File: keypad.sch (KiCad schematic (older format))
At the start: 19 parts, among them J1 Conn_01x04_Female, J3 B3FS-1002P, J4 USB_C_Receptacle_USB2.0, U1 ATMEGA32U4, Y1 Crystal_GND24

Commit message: first manufactured version, testing needed
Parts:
- J4: footprint Connector_USB:USB_C_Receptacle_Amphenol_12401548E4-2A_CircularHoles -> USB_C:Wuerth USB3.1 Type C Receptacle - Horizontal
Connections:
- wire segments 103 -> 101
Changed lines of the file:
@@
 	3900 4650 3900 4600
-Wire Wire Line
-	4200 4650 3900 4650
-Wire Wire Line
-	4200 4600 4200 4650
 Wire Wire Line
 	4900 3900 4800 3900
@@
 F 0 "J4" H 4305 4567 50  0000 C CNN
 F 1 "USB_C_Receptacle_USB2.0" H 4305 4476 50  0000 C CNN
-F 2 "Connector_USB:USB_C_Receptacle_Amphenol_12401548E4-2A_CircularHoles" H 4350 3700 50  0001 C CNN
+F 2 "USB_C:Wuerth USB3.1 Type C Receptacle - Horizontal" H 4350 3700 50  0001 C CNN
 F 3 "https://www.usb.org/sites/default/files/documents/usb_type-c.zip" H 4350 3700 50  0001 C CNN
 	1    4200 3700
@@
 	5850 4700 6500 4700
 Connection ~ 4900 3800
-Wire Wire Line
-	4200 4650 4200 4900
-Connection ~ 4200 4650
 Wire Wire Line
 	4200 4900 6550 4900
@@
 Wire Wire Line
 	6500 4700 6600 4700
+Wire Wire Line
+	4200 4600 4200 4900
 $EndSCHEMATC

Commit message: Auf STM32F303 Controller umgestiegen. RGB per Switch rausgeflogen.
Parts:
- removed C1, C2, C3, C4: 0.1u, Capacitor_SMD:C_0805_2012Metric_Pad1.15x1.40mm_HandSolder, symbol keyboard_parts:C
- removed C5: 4.7u, Capacitor_SMD:C_0805_2012Metric_Pad1.15x1.40mm_HandSolder, symbol keyboard_parts:C
- removed C6: 1u, Capacitor_SMD:C_0805_2012Metric_Pad1.15x1.40mm_HandSolder, symbol keyboard_parts:C
- removed C7, C8: 22p, Capacitor_SMD:C_0805_2012Metric_Pad1.15x1.40mm_HandSolder, symbol keyboard_parts:C
- removed J3: B3FS-1002P, SMD_Switch:B3FS-1002P, symbol smd_switch:B3FS-1002P
- removed J4: USB_C_Receptacle_USB2.0, USB_C:Wuerth USB3.1 Type C Receptacle - Horizontal, symbol Connector:USB_C_Receptacle_USB2.0
- removed R1, R4: 10k, Resistor_SMD:R_0805_2012Metric_Pad1.15x1.40mm_HandSolder, symbol keyboard_parts:R
- removed R10, R9: 56k, Resistor_SMD:R_0805_2012Metric_Pad1.15x1.40mm_HandSolder, symbol Device:R
- removed R2, R3: 22, Resistor_SMD:R_0805_2012Metric_Pad1.15x1.40mm_HandSolder, symbol keyboard_parts:R
- removed U1: ATMEGA32U4, Package_QFP:LQFP-44_10x10mm_P0.8mm, symbol keyboard_parts:ATMEGA32U4
- removed Y1: Crystal_GND24, Crystal:Crystal_SMD_Abracon_ABM8G-4Pin_3.2x2.5mm, symbol Device:Crystal_GND24
- added C1, C2, C3, C4, C8: 0.1u, Capacitor_SMD:C_0805_2012Metric_Pad1.15x1.40mm_HandSolder, symbol Device:C_Small
- added C10, C9: 10u, Capacitor_SMD:C_0805_2012Metric_Pad1.15x1.40mm_HandSolder, symbol Device:C_Small
- added C11: 4.7n, Capacitor_SMD:C_0805_2012Metric_Pad1.15x1.40mm_HandSolder, symbol Device:C_Small
- added C5: 4.7u, Capacitor_SMD:C_0805_2012Metric_Pad1.15x1.40mm_HandSolder, symbol Device:C_Small
- added C6, C7: 18p, Capacitor_SMD:C_0805_2012Metric_Pad1.15x1.40mm_HandSolder, symbol Device:C_Small
- added D1: POWER_LED, LED_SMD:LED_0805_2012Metric_Pad1.15x1.40mm_HandSolder, symbol Device:LED
- added J3: USB_C_Receptacle_USB2.0, USB_C:USB C HRQ low cost, symbol Connector:USB_C_Receptacle_USB2.0
- added R1: 1.5k, Resistor_SMD:R_0805_2012Metric_Pad1.15x1.40mm_HandSolder, symbol Device:R_Small
- added R10, R11: 22, Resistor_SMD:R_0805_2012Metric_Pad1.15x1.40mm_HandSolder, symbol Device:R_Small
- added R4: 10k, Resistor_SMD:R_0805_2012Metric_Pad1.15x1.40mm_HandSolder, symbol Device:R_Small
- added R5: 330, Resistor_SMD:R_0805_2012Metric_Pad1.15x1.40mm_HandSolder, symbol Device:R_Small
- added R6: 1M, Resistor_SMD:R_0805_2012Metric_Pad1.15x1.40mm_HandSolder, symbol Device:R_Small
- added R7, R8: 5.1k, Resistor_SMD:R_0805_2012Metric_Pad1.15x1.40mm_HandSolder, symbol Device:R_Small
- added SW1, SW2: SW_Push_Dual, SMD_Switch:B3FS-1002P, symbol Switch:SW_Push_Dual
- added U1: STM32F303C6Tx, Package_QFP:LQFP-48_7x7mm_P0.5mm, symbol MCU_ST_STM32F3:STM32F303C6Tx
- added U2: MCP1804x-3302xOT, Package_TO_SOT_SMD:SOT-23-5_HandSoldering, symbol keypad:MCP1804x-3302xOT
- added Y1: A7 8MHz, Crystal:Crystal_SMD_5032-2Pin_5.0x3.2mm_HandSoldering, symbol Device:Crystal
- J1: footprint Connector_PinHeader_1.00mm:PinHeader_1x04_P1.00mm_Vertical -> Connector_PinHeader_2.00mm:PinHeader_1x04_P2.00mm_Vertical
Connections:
- net labels added: +3.3V, BOOT, NRST, OSC_IN, OSC_OUT, USB_N, USB_P, VBUS
- net labels removed: CC1, CC2, USB_D+, USB_D-, USB_GND
- wire segments 101 -> 130
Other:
- note added: "5?\n"
- note added: "vor oder hinter R?\n"

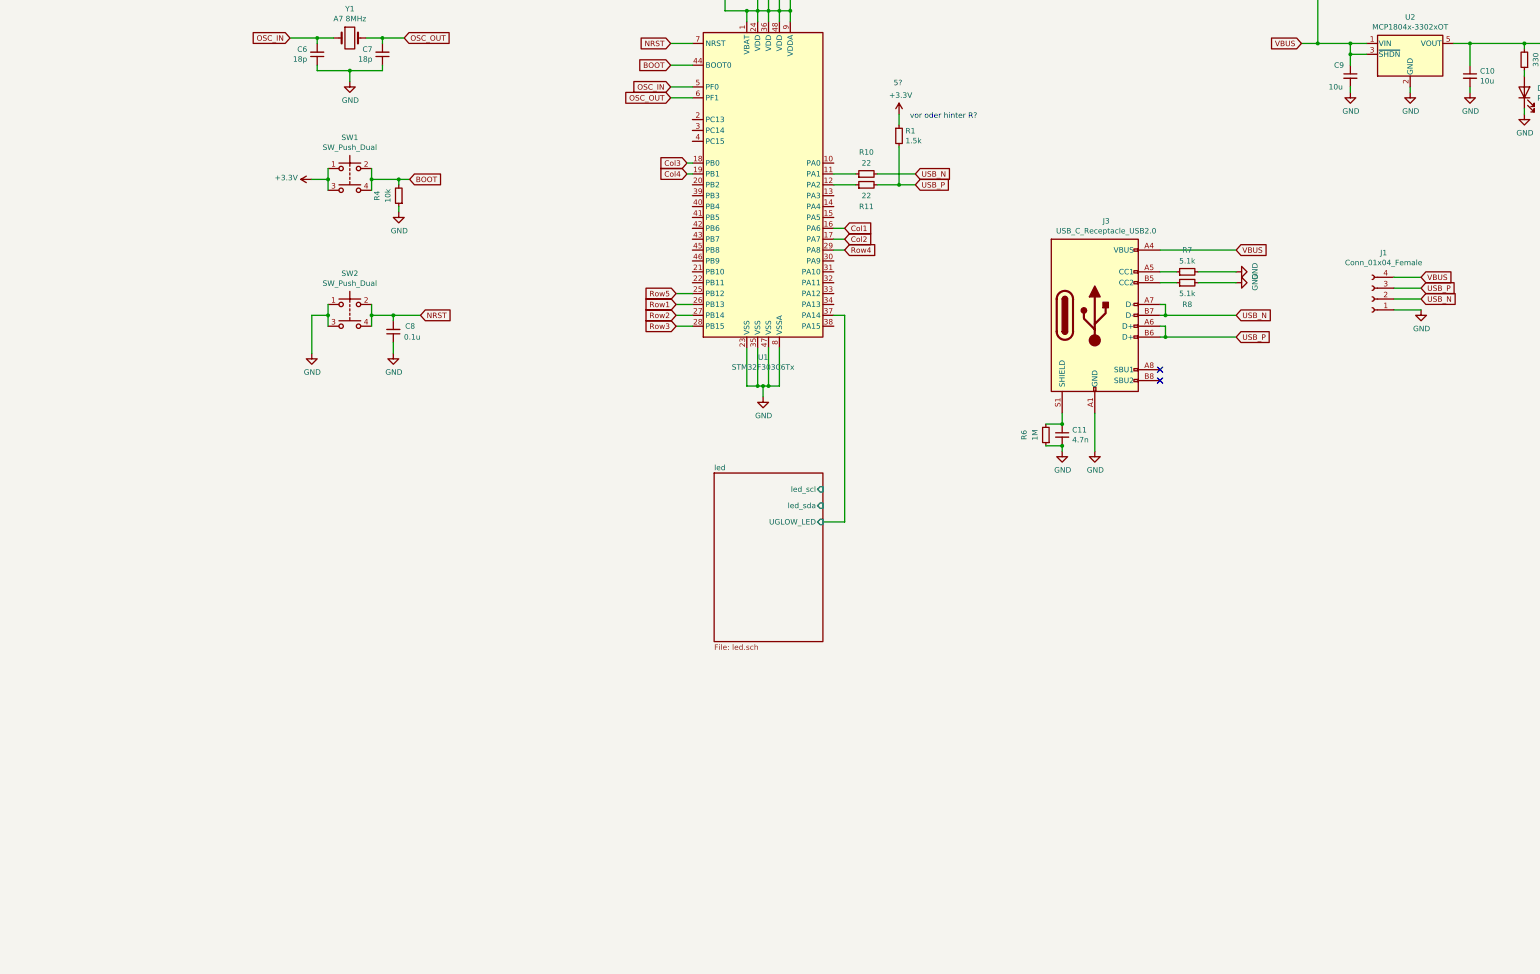
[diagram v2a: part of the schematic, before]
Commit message: USB war an falschem Pin. Fixed! Boot und Reset geaendert. Anderer Resetbutton
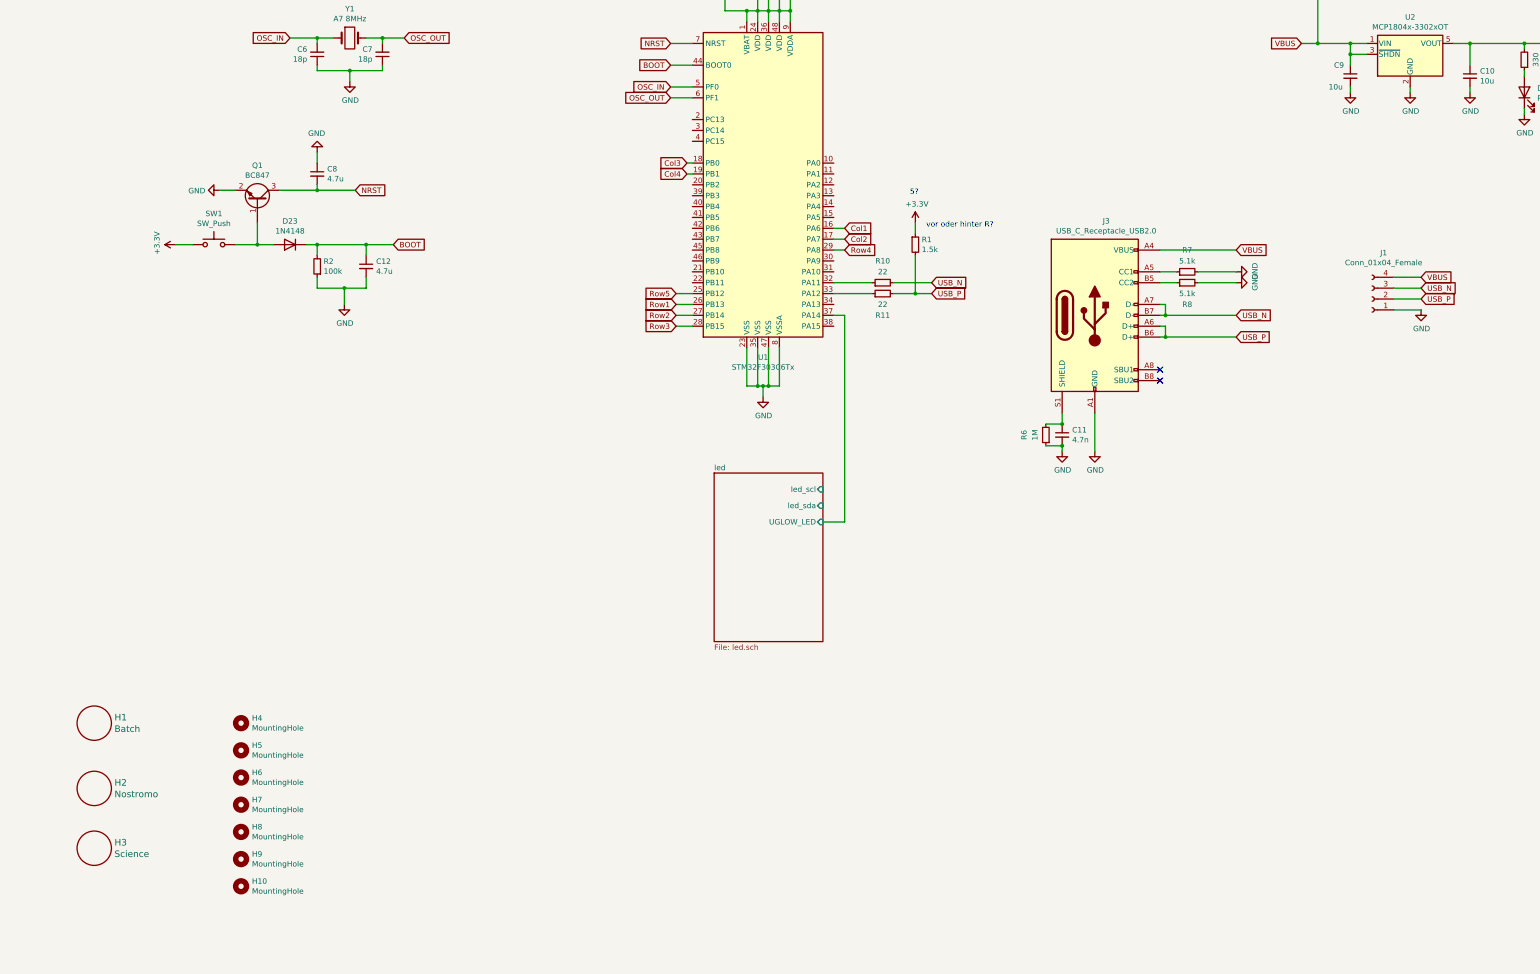
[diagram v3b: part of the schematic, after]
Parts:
- removed R4: 10k, Resistor_SMD:R_0805_2012Metric_Pad1.15x1.40mm_HandSolder, symbol Device:R_Small
- removed SW1, SW2: SW_Push_Dual, SMD_Switch:B3FS-1002P, symbol Switch:SW_Push_Dual
- added C12: 4.7u, Capacitor_SMD:C_0805_2012Metric_Pad1.15x1.40mm_HandSolder, symbol Device:C_Small
- added D23: 1N4148, Diode_SMD:D_0805_2012Metric_Pad1.15x1.40mm_HandSolder, symbol Device:D
- added H1: Batch, decals:nostromo_batch, symbol keebio:Hole
- added H10, H4, H5, H6, H7, H8, H9: MountingHole, MountingHole:MountingHole_2.2mm_M2, symbol Mechanical:MountingHole
- added H2: Nostromo, decals:nostromo, symbol keebio:Hole
- added H3: Science, decals:science_badge, symbol keebio:Hole
- added Q1: BC847, Package_TO_SOT_SMD:SOT-23, symbol Transistor_BJT:BC847
- added R2: 100k, Resistor_SMD:R_0805_2012Metric_Pad1.15x1.40mm_HandSolder, symbol Device:R_Small
- added SW1: SW_Push, Button_Switch_SMD:SW_SPST_B3U-1000P, symbol Switch:SW_Push
- C8: value 0.1u -> 4.7u
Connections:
- net +3V3: now also SW1.1
- net BOOT: now also C12.1, D23.1 (K), R2.2
- net GND: now also C12.2, Q1.2 (E), R2.1
- net NRST: now also Q1.3 (C)
- net USB_N: now also J1.3 (Pin_3); no longer J1.2 (Pin_2)
- net USB_P: now also J1.2 (Pin_2); no longer J1.3 (Pin_3)
- net at U1.11 (PA1): no longer R10.1
- net at U1.12 (PA2): no longer R11.1
- net at U1.32 (PA11): now also R10.1
- net at U1.33 (PA12): now also R11.1
- new net: D23.2 (A), Q1.1 (B), SW1.2
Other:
- moved on the sheet: R1, R10, R11

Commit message: - Quarz geaendert - Debug LED hinzugefügt
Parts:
- removed R8: 5.1k, Resistor_SMD:R_0805_2012Metric_Pad1.15x1.40mm_HandSolder, symbol Device:R_Small
- added D24: 1N4148, Diode_SMD:D_0805_2012Metric_Pad1.15x1.40mm_HandSolder, symbol Device:D
- added D25: POWER_LED, LED_SMD:LED_0805_2012Metric_Pad1.15x1.40mm_HandSolder, symbol Device:LED
- added R3: 330, Resistor_SMD:R_0805_2012Metric_Pad1.15x1.40mm_HandSolder, symbol Device:R_Small
- C1, C2, C3: value 0.1u -> 100n
- C12, C8: value 4.7u -> 4.7n
- C4: value 0.1u -> 1u
- C6, C7: value 18p -> 22p
- J3: symbol Connector:USB_C_Receptacle_USB2.0 -> keypad-rescue:USB_C_Receptacle_USB2.0-Connector
- Y1: footprint Crystal:Crystal_SMD_5032-2Pin_5.0x3.2mm_HandSoldering -> Crystal:Crystal_SMD_5032-4Pin_5.0x3.2mm; symbol Device:Crystal -> Device:Crystal_GND24
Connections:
- net +3V3: now also D24.2 (A); no longer R1.1
- net +5V: now also R1.1, D24.1 (K)
- net GND: now also Y1.2, Y1.4, D25.1 (K)
- net OSC_OUT: now also Y1.3; no longer Y1.2
- net USB_P: no longer R1.2
- net at U1.13 (PA3): now also R3.2
- net at R11.1, U1.33 (PA12): now also R1.2
- net at J3.A5 (CC1), R7.1: now also J3.B5 (CC2)
- new net: D25.2 (A), R3.1
- no-connect marks 2 -> 24
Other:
- moved on the sheet: R10, R11, R7
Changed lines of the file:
@@
 EESchema Schematic File Version 4
 LIBS:keypad-cache
-EELAYER 26 0
+EELAYER 29 0
 EELAYER END
 $Descr A3 16535 11693
@@
 P 7850 1750
 F 0 "C1" H 7942 1796 50  0000 L CNN
-F 1 "0.1u" H 7942 1705 50  0000 L CNN
+F 1 "100n" H 7942 1705 50  0000 L CNN
 F 2 "Capacitor_SMD:C_0805_2012Metric_Pad1.15x1.40mm_HandSolder" H 7850 1750 50  0001 C CNN
 F 3 "~" H 7850 1750 50  0001 C CNN
@@
 P 7950 1550
 F 0 "C2" H 8042 1596 50  0000 L CNN
-F 1 "0.1u" H 8042 1505 50  0000 L CNN
+F 1 "100n" H 8042 1505 50  0000 L CNN
 F 2 "Capacitor_SMD:C_0805_2012Metric_Pad1.15x1.40mm_HandSolder" H 7950 1550 50  0001 C CNN
 F 3 "~" H 7950 1550 50  0001 C CNN
@@
 P 8050 1350
 F 0 "C3" H 8142 1396 50  0000 L CNN
-F 1 "0.1u" H 8142 1305 50  0000 L CNN
+F 1 "100n" H 8142 1305 50  0000 L CNN
 F 2 "Capacitor_SMD:C_0805_2012Metric_Pad1.15x1.40mm_HandSolder" H 8050 1350 50  0001 C CNN
 F 3 "~" H 8050 1350 50  0001 C CNN
@@
 P 8150 1150
 F 0 "C4" H 8242 1196 50  0000 L CNN
-F 1 "0.1u" H 8242 1105 50  0000 L CNN
+F 1 "1u" H 8242 1105 50  0000 L CNN
 F 2 "Capacitor_SMD:C_0805_2012Metric_Pad1.15x1.40mm_HandSolder" H 8150 1150 50  0001 C CNN
 F 3 "~" H 8150 1150 50  0001 C CNN
@@
 	1    0    0    -1
 $EndComp
-Wire Wire Line
-	9300 4200 9300 4550
-$Comp
-L power:+3.3V #PWR05
+$Comp
+L power:+5V #PWR05
 U 1 1 5C5A88A8
 P 9300 3900
 F 0 "#PWR05" H 9300 3750 50  0001 C CNN
-F 1 "+3.3V" H 9315 4073 50  0000 C CNN
+F 1 "+5V" H 9315 4073 50  0000 C CNN
 F 2 "" H 9300 3900 50  0001 C CNN
 F 3 "" H 9300 3900 50  0001 C CNN
@@
 $EndComp
 $Comp
-L Device:Crystal Y1
+L Device:Crystal_GND24 Y1
 U 1 1 5C5AEF4D
 P 4100 2200
 F 0 "Y1" H 4100 2468 50  0000 C CNN
 F 1 "A7 8MHz" H 4100 2377 50  0000 C CNN
-F 2 "Crystal:Crystal_SMD_5032-2Pin_5.0x3.2mm_HandSoldering" H 4100 2200 50  0001 C CNN
+F 2 "Crystal:Crystal_SMD_5032-4Pin_5.0x3.2mm" H 4100 2200 50  0001 C CNN
 F 3 "~" H 4100 2200 50  0001 C CNN
 	1    4100 2200
@@
 P 3800 2350
 F 0 "C6" H 3708 2304 50  0000 R CNN
-F 1 "18p" H 3708 2395 50  0000 R CNN
+F 1 "22p" H 3708 2395 50  0000 R CNN
 F 2 "Capacitor_SMD:C_0805_2012Metric_Pad1.15x1.40mm_HandSolder" H 3800 2350 50  0001 C CNN
 F 3 "~" H 3800 2350 50  0001 C CNN
@@
 P 4400 2350
 F 0 "C7" H 4308 2304 50  0000 R CNN
-F 1 "18p" H 4308 2395 50  0000 R CNN
+F 1 "22p" H 4308 2395 50  0000 R CNN
 F 2 "Capacitor_SMD:C_0805_2012Metric_Pad1.15x1.40mm_HandSolder" H 4400 2350 50  0001 C CNN
 F 3 "~" H 4400 2350 50  0001 C CNN
@@
 Text GLabel 7050 2750 0    50   Input ~ 0
 OSC_OUT
-Text GLabel 9450 4550 2    50   Input ~ 0
+Text GLabel 9800 4550 2    50   Input ~ 0
 USB_P
-Text GLabel 9450 4450 2    50   Input ~ 0
+Text GLabel 9800 4450 2    50   Input ~ 0
 USB_N
 Wire Wire Line
@@
 $EndComp
 $Comp
-L Connector:USB_C_Receptacle_USB2.0 J3
+L keypad-rescue:USB_C_Receptacle_USB2.0-Connector J3
 U 1 1 5C62BE00
 P 10950 4750
@@
 	11600 4950 11550 4950
 Wire Wire Line
-	11550 4350 11700 4350
-Wire Wire Line
-	11550 4450 11700 4450
+	11550 4350 11800 4350
 $Comp
 L Device:R_Small R7
 U 1 1 5C6592C5
-P 11800 4350
-F 0 "R7" V 12000 4350 50  0000 C CNN
-F 1 "5.1k" V 11900 4350 50  0000 C CNN
-F 2 "Resistor_SMD:R_0805_2012Metric_Pad1.15x1.40mm_HandSolder" H 11800 4350 50  0001 C CNN
-F 3 "~" H 11800 4350 50  0001 C CNN
-	1    11800 4350
-	0    -1   -1   0
-$EndComp
-$Comp
-L Device:R_Small R8
-U 1 1 5C6593B0
-P 11800 4450
-F 0 "R8" V 11600 4450 50  0000 C CNN
-F 1 "5.1k" V 11700 4450 50  0000 C CNN
-F 2 "Resistor_SMD:R_0805_2012Metric_Pad1.15x1.40mm_HandSolder" H 11800 4450 50  0001 C CNN
-F 3 "~" H 11800 4450 50  0001 C CNN
-	1    11800 4450
+P 12050 4350
+F 0 "R7" V 12250 4350 50  0000 C CNN
+F 1 "5.1k" V 12150 4350 50  0000 C CNN
+F 2 "Resistor_SMD:R_0805_2012Metric_Pad1.15x1.40mm_HandSolder" H 12050 4350 50  0001 C CNN
+F 3 "~" H 12050 4350 50  0001 C CNN
+	1    12050 4350
 	0    -1   -1   0
 $EndComp
@@
 L Device:R_Small R10
 U 1 1 5C66AC4F
-P 9000 4450
-F 0 "R10" V 9200 4450 50  0000 C CNN
-F 1 "22" V 9100 4450 50  0000 C CNN
-F 2 "Resistor_SMD:R_0805_2012Metric_Pad1.15x1.40mm_HandSolder" H 9000 4450 50  0001 C CNN
-F 3 "~" H 9000 4450 50  0001 C CNN
-	1    9000 4450
+P 9600 4450
+F 0 "R10" V 9800 4450 50  0000 C CNN
+F 1 "22" V 9700 4450 50  0000 C CNN
+F 2 "Resistor_SMD:R_0805_2012Metric_Pad1.15x1.40mm_HandSolder" H 9600 4450 50  0001 C CNN
+F 3 "~" H 9600 4450 50  0001 C CNN
+	1    9600 4450
 	0    -1   -1   0
 $EndComp
@@
 L Device:R_Small R11
 U 1 1 5C66ACC9
-P 9000 4550
-F 0 "R11" V 8800 4550 50  0000 C CNN
-F 1 "22" V 8900 4550 50  0000 C CNN
-F 2 "Resistor_SMD:R_0805_2012Metric_Pad1.15x1.40mm_HandSolder" H 9000 4550 50  0001 C CNN
-F 3 "~" H 9000 4550 50  0001 C CNN
-	1    9000 4550
+P 9600 4550
+F 0 "R11" V 9400 4550 50  0000 C CNN
+F 1 "22" V 9500 4550 50  0000 C CNN
+F 2 "Resistor_SMD:R_0805_2012Metric_Pad1.15x1.40mm_HandSolder" H 9600 4550 50  0001 C CNN
+F 3 "~" H 9600 4550 50  0001 C CNN
+	1    9600 4550
 	0    -1   -1   0
 $EndComp
@@
 	11550 4150 12250 4150
 Wire Wire Line
-	11900 4350 12250 4350
-Wire Wire Line
-	11900 4450 12250 4450
+	12150 4350 12250 4350
 NoConn ~ 11550 5250
 NoConn ~ 11550 5350
@@
 	0    -1   -1   0
 $EndComp
-$Comp
-L power:GND #PWR022
-U 1 1 5C687CA4
-P 12250 4450
-F 0 "#PWR022" H 12250 4200 50  0001 C CNN
-F 1 "GND" H 12255 4277 50  0000 C CNN
-F 2 "" H 12250 4450 50  0001 C CNN
-F 3 "" H 12250 4450 50  0001 C CNN
-	1    12250 4450
-	0    -1   -1   0
-$EndComp
 Text GLabel 12250 4950 2    50   Input ~ 0
 USB_P
@@
 $EndComp
 Wire Wire Line
-	9100 4450 9450 4450
-Wire Wire Line
-	9100 4550 9300 4550
+	9700 4450 9800 4450
 Wire Wire Line
 	11600 4750 12250 4750
@@
 Wire Wire Line
 	7200 3450 7250 3450
-Connection ~ 9300 4550
-Wire Wire Line
-	9300 4550 9450 4550
 Text Notes 9400 3950 0    50   ~ 0
 vor oder hinter R?\n
@@
 	8650 6650 8450 6650
 Wire Wire Line
-	8550 4450 8900 4450
-Wire Wire Line
-	8550 4550 8900 4550
+	8550 4450 9500 4450
+Wire Wire Line
+	8550 4550 9300 4550
 $Comp
 L Transistor_BJT:BC847 Q1
@@
 P 3800 3450
 F 0 "C8" H 3892 3496 50  0000 L CNN
-F 1 "4.7u" H 3892 3405 50  0000 L CNN
+F 1 "4.7n" H 3892 3405 50  0000 L CNN
 F 2 "Capacitor_SMD:C_0805_2012Metric_Pad1.15x1.40mm_HandSolder" H 3800 3450 50  0001 C CNN
 F 3 "~" H 3800 3450 50  0001 C CNN
@@
 P 4250 4300
 F 0 "C12" H 4342 4346 50  0000 L CNN
-F 1 "4.7u" H 4342 4255 50  0000 L CNN
+F 1 "4.7n" H 4342 4255 50  0000 L CNN
 F 2 "Capacitor_SMD:C_0805_2012Metric_Pad1.15x1.40mm_HandSolder" H 4250 4300 50  0001 C CNN
 F 3 "~" H 4250 4300 50  0001 C CNN
@@
 	1    0    0    -1
 $EndComp
+Wire Wire Line
+	9700 4550 9800 4550
+Wire Wire Line
+	9300 4200 9300 4550
+Connection ~ 9300 4550
+Wire Wire Line
+	9300 4550 9500 4550
+Wire Wire Line
+	4100 2400 4100 2500
+$Comp
+L power:GND #PWR0103
+U 1 1 5CBD4C96
+P 4100 1750
+F 0 "#PWR0103" H 4100 1500 50  0001 C CNN
+F 1 "GND" H 4105 1577 50  0000 C CNN
+F 2 "" H 4100 1750 50  0001 C CNN
+F 3 "" H 4100 1750 50  0001 C CNN
+	1    4100 1750
+	-1   0    0    1
+$EndComp
+Wire Wire Line
+	4100 1750 4100 2000
+Wire Wire Line
+	11550 4450 11800 4450
+Wire Wire Line
+	11800 4450 11800 4350
+Connection ~ 11800 4350
+Wire Wire Line
+	11800 4350 11950 4350
+NoConn ~ 7250 2950
+NoConn ~ 7250 3050
+NoConn ~ 7250 3150
+NoConn ~ 7250 3550
+NoConn ~ 7250 3650
+NoConn ~ 7250 3750
+NoConn ~ 7250 3850
+NoConn ~ 7250 3950
+NoConn ~ 7250 4050
+NoConn ~ 7250 4150
+NoConn ~ 7250 4250
+NoConn ~ 7250 4350
+NoConn ~ 7250 4450
+NoConn ~ 8550 3350
+NoConn ~ 8550 3450
+NoConn ~ 8550 3550
+NoConn ~ 8550 3750
+NoConn ~ 8550 3850
+NoConn ~ 8550 4250
+NoConn ~ 8550 4350
+NoConn ~ 8550 4650
+NoConn ~ 8550 4850
+$Comp
+L Device:D D24
+U 1 1 5CC60B23
+P 13850 1700
+F 0 "D24" H 13850 1484 50  0000 C CNN
+F 1 "1N4148" H 13850 1575 50  0000 C CNN
+F 2 "Diode_SMD:D_0805_2012Metric_Pad1.15x1.40mm_HandSolder" H 13850 1700 50  0001 C CNN
+F 3 "~" H 13850 1700 50  0001 C CNN
+	1    13850 1700
+	1    0    0    -1
+$EndComp
+Wire Wire Line
+	14000 1700 14400 1700
+Wire Wire Line
+	14400 1700 14400 2250
+Wire Wire Line
+	13700 1700 13300 1700
+Wire Wire Line
+	13300 1700 13300 2250
+$Comp
+L Device:R_Small R3
+U 1 1 5CC6F633
+P 8850 3350
+F 0 "R3" V 8654 3350 50  0000 C CNN
+F 1 "330" V 8745 3350 50  0000 C CNN
+F 2 "Resistor_SMD:R_0805_2012Metric_Pad1.15x1.40mm_HandSolder" H 8850 3350 50  0001 C CNN
+F 3 "~" H 8850 3350 50  0001 C CNN
+	1    8850 3350
+	0    1    1    0
+$EndComp
+$Comp
+L Device:LED D25
+U 1 1 5CC6F63D
+P 9150 3350
+F 0 "D25" V 9188 3232 50  0000 R CNN
+F 1 "POWER_LED" V 9097 3232 50  0000 R CNN
+F 2 "LED_SMD:LED_0805_2012Metric_Pad1.15x1.40mm_HandSolder" H 9150 3350 50  0001 C CNN
+F 3 "~" H 9150 3350 50  0001 C CNN
+	1    9150 3350
+	-1   0    0    1
+$EndComp
+$Comp
+L power:GND #PWR0104
+U 1 1 5CC6F647
+P 9350 3350
+F 0 "#PWR0104" H 9350 3100 50  0001 C CNN
+F 1 "GND" H 9355 3177 50  0000 C CNN
+F 2 "" H 9350 3350 50  0001 C CNN
+F 3 "" H 9350 3350 50  0001 C CNN
+	1    9350 3350
+	0    -1   -1   0
+$EndComp
+Wire Wire Line
+	8950 3350 9000 3350
+Wire Wire Line
+	9300 3350 9350 3350
+Wire Wire Line
+	8550 3650 8700 3650
+Wire Wire Line
+	8700 3650 8700 3350
+Wire Wire Line
+	8700 3350 8750 3350
 $EndSCHEMATC
